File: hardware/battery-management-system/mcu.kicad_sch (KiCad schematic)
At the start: 32 parts, among them J7 ARM-JTAG-SWD, Q6 DMN3404L, Q7 DMN3404L, Q8 DMN3404L, U6 AT24C512C, U7 NCT75DR2G, U8 STM32L071CZTx

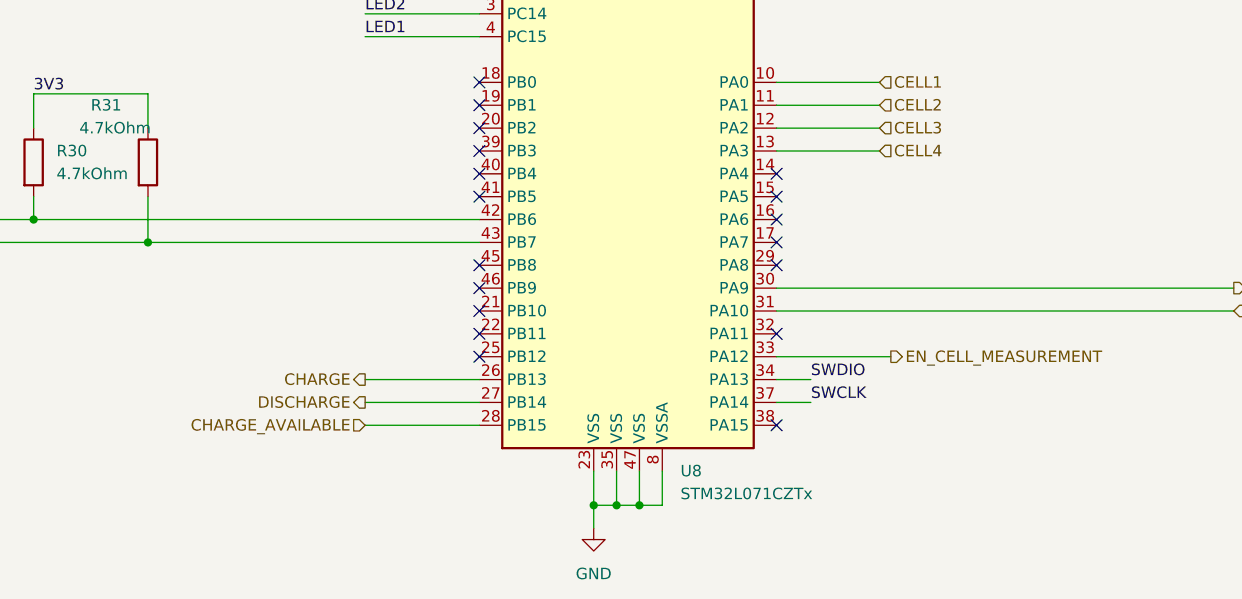
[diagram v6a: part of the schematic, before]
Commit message: finish cell balancing schematic
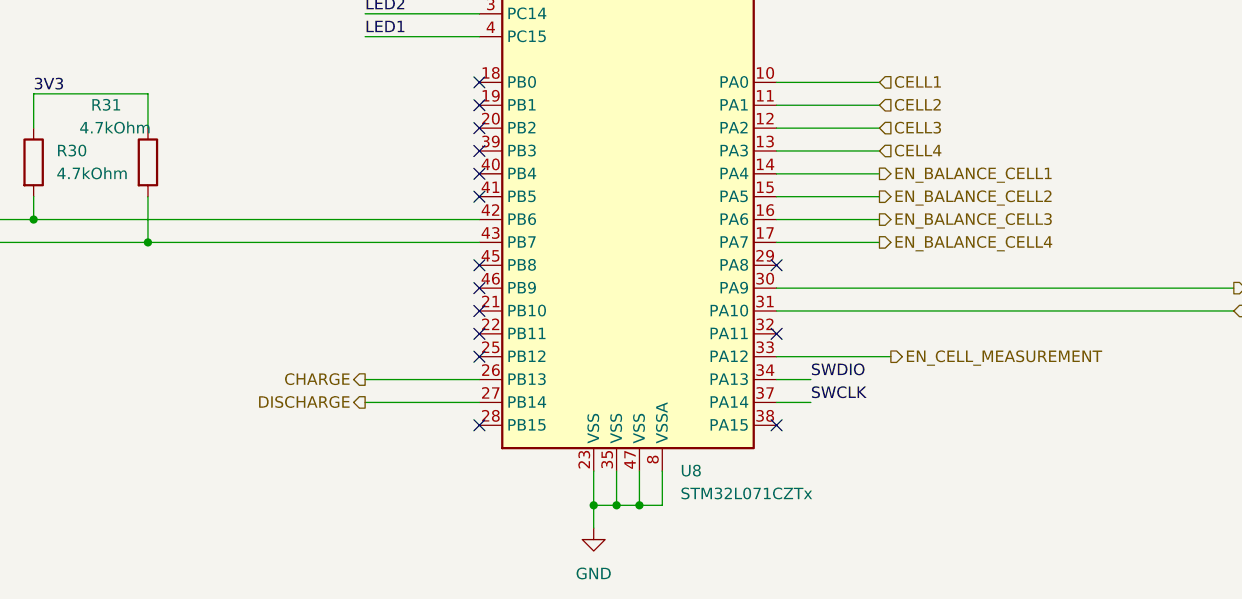
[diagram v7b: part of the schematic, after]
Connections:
- net EN_BALANCE_CELL1: now reaches U8.14 (PA4)
- net EN_BALANCE_CELL2: now reaches U8.15 (PA5)
- net EN_BALANCE_CELL3: now reaches U8.16 (PA6)
- net EN_BALANCE_CELL4: now reaches U8.17 (PA7)
- net CHARGE_AVAILABLE: no longer names the net of U8.28 (PB15)
- no-connect marks 24 -> 21
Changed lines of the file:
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@@
 	)
 	(no_connect
-		(at 27.94 81.28)
+		(at 185.42 104.14)
 	)
 	(no_connect
-		(at 218.44 76.2)
+		(at 27.94 81.28)
 	)
 	(no_connect
@@
 	)
 	(no_connect
-		(at 218.44 83.82)
-	)
-	(no_connect
 		(at 185.42 76.2)
 	)
@@
 	)
 	(no_connect
-		(at 218.44 81.28)
-	)
-	(no_connect
 		(at 218.44 104.14)
 	)
@@
 	)
 	(no_connect
-		(at 218.44 78.74)
-	)
-	(no_connect
 		(at 185.42 48.26)
 	)
@@
 	(wire
 		(pts
+			(xy 218.44 83.82) (xy 229.87 83.82)
+		)
+		(stroke
+			(width 0)
+			(type default)
+		)
+	)
+	(wire
+		(pts
 			(xy 73.66 185.42) (xy 73.66 186.69)
 		)
@@
 	(wire
 		(pts
+			(xy 218.44 78.74) (xy 229.87 78.74)
+		)
+		(stroke
+			(width 0)
+			(type default)
+		)
+	)
+	(wire
+		(pts
 			(xy 90.17 31.75) (xy 102.87 31.75)
 		)
@@
 	(wire
 		(pts
+			(xy 218.44 76.2) (xy 229.87 76.2)
+		)
+		(stroke
+			(width 0)
+			(type default)
+		)
+	)
+	(wire
+		(pts
 			(xy 203.2 113.03) (xy 205.74 113.03)
 		)
@@
 	(wire
 		(pts
+			(xy 218.44 81.28) (xy 229.87 81.28)
+		)
+		(stroke
+			(width 0)
+			(type default)
+		)
+	)
+	(wire
+		(pts
 			(xy 129.54 44.45) (xy 129.54 46.99)
 		)
@@
 	(wire
 		(pts
-			(xy 172.72 104.14) (xy 185.42 104.14)
-		)
-		(stroke
-			(width 0)
-			(type default)
-		)
-	)
-	(wire
-		(pts
 			(xy 83.82 96.52) (xy 83.82 99.06)
 		)
@@
 		)
 	)
-	(hierarchical_label "CHARGE_AVAILABLE"
-		(shape input)
-		(at 172.72 104.14 180)
+	(hierarchical_label "EN_BALANCE_CELL4"
+		(shape output)
+		(at 229.87 83.82 0)
 		(fields_autoplaced yes)
 		(effects
@@
 				(size 1.27 1.27)
 			)
-			(justify right)
+			(justify left)
 		)
 	)
@@
 		)
 	)
+	(hierarchical_label "EN_BALANCE_CELL1"
+		(shape output)
+		(at 229.87 76.2 0)
+		(fields_autoplaced yes)
+		(effects
+			(font
+				(size 1.27 1.27)
+			)
+			(justify left)
+		)
+	)
+	(hierarchical_label "EN_BALANCE_CELL2"
+		(shape output)
+		(at 229.87 78.74 0)
+		(fields_autoplaced yes)
+		(effects
+			(font
+				(size 1.27 1.27)
+			)
+			(justify left)
+		)
+	)
+	(hierarchical_label "EN_BALANCE_CELL3"
+		(shape output)
+		(at 229.87 81.28 0)
+		(fields_autoplaced yes)
+		(effects
+			(font
+				(size 1.27 1.27)
+			)
+			(justify left)
+		)
+	)
 	(symbol
 		(lib_id "benediktibk:C_1uF_SMD_0603_50V_10%")
@@
 			)
 		)
-		(property "Description" ""
+		(property "Description" "Unpolarized capacitor"
 			(at 129.54 40.64 0)
 			(effects
@@
 			)
 		)
-		(property "Description" ""
+		(property "Description" "Special symbol for telling ERC where power comes from"
 			(at 53.34 31.75 0)
 			(effects
@@
 			)
 		)
-		(property "Description" ""
+		(property "Description" "Resistor"
 			(at 97.79 186.69 0)
 			(effects
@@
 			)
 		)
-		(property "Description" ""
+		(property "Description" "Resistor"
 			(at 36.83 168.91 0)
 			(effects
@@
 			)
 		)
-		(property "Description" ""
+		(property "Description" "n-MOSFET transistor, drain/gate/source"
 			(at 34.29 180.34 0)
 			(effects
@@
 			)
 		)
-		(property "Description" ""
+		(property "Description" "Unpolarized capacitor"
 			(at 96.52 90.17 0)
 			(effects
@@
 			)
 		)
-		(property "Description" ""
+		(property "Description" "Light emitting diode"
 			(at 109.22 158.75 0)
 			(effects
@@
 			)
 		)
-		(property "Description" ""
+		(property "Description" "Unpolarized capacitor"
 			(at 64.77 40.64 0)
 			(effects
@@
 			)
 		)
-		(property "Description" ""
+		(property "Description" "Special symbol for telling ERC where power comes from"
 			(at 129.54 31.75 0)
 			(effects
@@
 			)
 		)
-		(property "Description" ""
+		(property "Description" "n-MOSFET transistor, drain/gate/source"
 			(at 106.68 180.34 0)
 			(effects
@@
 			)
 		)
-		(property "Description" ""
+		(property "Description" "Power symbol creates a global label with name \"GND\" , ground"
 			(at 36.83 189.23 0)
 			(effects
@@
 			)
 		)
-		(property "Description" ""
+		(property "Description" "Resistor"
 			(at 177.8 43.18 0)
 			(effects
@@
 			)
 		)
-		(property "Description" ""
+		(property "Description" "Power symbol creates a global label with name \"GND\" , ground"
 			(at 73.66 189.23 0)
 			(effects
@@
 			)
 		)
-		(property "Description" ""
+		(property "Description" "Power symbol creates a global label with name \"GND\" , ground"
 			(at 74.93 138.43 0)
 			(effects
@@
 			)
 		)
-		(property "Description" ""
+		(property "Description" "Power symbol creates a global label with name \"GND\" , ground"
 			(at 129.54 49.53 0)
 			(effects
@@
 			)
 		)
-		(property "Description" ""
+		(property "Description" "Resistor"
 			(at 135.89 74.93 0)
 			(effects
@@
 			)
 		)
-		(property "Description" ""
+		(property "Description" "Resistor"
 			(at 73.66 168.91 0)
 			(effects
@@
 			)
 		)
-		(property "Description" ""
+		(property "Description" "Unpolarized capacitor"
 			(at 90.17 40.64 0)
 			(effects
@@
 			)
 		)
-		(property "Description" ""
+		(property "Description" "Single Pole Single Throw (SPST) switch"
 			(at 83.82 91.44 0)
 			(effects
@@
 			)
 		)
-		(property "Description" ""
+		(property "Description" "Power symbol creates a global label with name \"GND\" , ground"
 			(at 109.22 189.23 0)
 			(effects
@@
 			)
 		)
-		(property "Description" ""
+		(property "Description" "Power symbol creates a global label with name \"GND\" , ground"
 			(at 24.13 86.36 0)
 			(effects
@@
 			)
 		)
-		(property "Description" ""
+		(property "Description" "Unpolarized capacitor"
 			(at 77.47 40.64 0)
 			(effects
@@
 			)
 		)
-		(property "Description" ""
+		(property "Description" "Unpolarized capacitor"
 			(at 116.84 40.64 0)
 			(effects
@@
 			)
 		)
-		(property "Description" ""
+		(property "Description" "Resistor"
 			(at 62.23 186.69 0)
 			(effects
@@
 			)
 		)
-		(property "Description" ""
+		(property "Description" "Resistor"
 			(at 25.4 186.69 0)
 			(effects
@@
 			)
 		)
-		(property "Description" ""
+		(property "Description" "Resistor"
 			(at 148.59 74.93 0)
 			(effects
@@
 			)
 		)
-		(property "Description" ""
+		(property "Description" "Power symbol creates a global label with name \"GND\" , ground"
 			(at 198.12 115.57 0)
 			(effects
@@
 			)
 		)
-		(property "Description" ""
+		(property "Description" "n-MOSFET transistor, drain/gate/source"
 			(at 71.12 180.34 0)
 			(effects
@@
 			)
 		)
-		(property "Description" ""
+		(property "Description" "Unpolarized capacitor"
 			(at 74.93 123.19 0)
 			(effects
@@
 			)
 		)
-		(property "Description" ""
+		(property "Description" "ARM Cortex-M0+ MCU, 192KB flash, 20KB RAM, 32MHz, 1.65-3.6V, 37 GPIO, LQFP-48"
 			(at 203.2 71.12 0)
 			(effects
@@
 			)
 		)
-		(property "Description" ""
+		(property "Description" "Power symbol creates a global label with name \"GND\" , ground"
 			(at 148.59 46.99 0)
 			(effects
@@
 			)
 		)
-		(property "Description" ""
+		(property "Description" "Light emitting diode"
 			(at 73.66 158.75 0)
 			(effects
@@
 			)
 		)
-		(property "Description" ""
+		(property "Description" "Light emitting diode"
 			(at 36.83 158.75 0)
 			(effects
@@
 			)
 		)
-		(property "Description" ""
+		(property "Description" "Power symbol creates a global label with name \"GND\" , ground"
 			(at 30.48 140.97 0)
 			(effects
@@
 			)
 		)
-		(property "Description" ""
+		(property "Description" "Resistor"
 			(at 109.22 168.91 0)
 			(effects
@@
 			)
 		)
-		(property "Description" ""
+		(property "Description" "I2C Serial EEPROM, 2Kb, SOT-23"
 			(at 93.98 124.46 0)
 			(effects
@@
 			)
 		)
-		(property "Description" ""
+		(property "Description" "Resistor"
 			(at 80.01 69.85 0)
 			(effects
@@
 			)
 		)
-		(property "Description" ""
+		(property "Description" "Power symbol creates a global label with name \"GND\" , ground"
 			(at 53.34 49.53 0)
 			(effects
@@
 			)
 		)
-		(property "Description" ""
+		(property "Description" "I2C Serial EEPROM, 2Kb, SOT-23"
 			(at 49.53 123.19 0)
 			(effects
@@
 			)
 		)
-		(property "Description" ""
+		(property "Description" "Unpolarized capacitor"
 			(at 30.48 121.92 0)
 			(effects
@@
 			)
 		)
-		(property "Description" ""
+		(property "Description" "Ferrite bead"
 			(at 110.49 31.75 0)
 			(effects
@@
 			)
 		)
-		(property "Description" ""
+		(property "Description" "Unpolarized capacitor"
 			(at 53.34 40.64 0)
 			(effects
@@
 			)
 		)
-		(property "Description" ""
+		(property "Description" "Unpolarized capacitor"
 			(at 102.87 40.64 0)
 			(effects
@@
 			)
 		)
-		(property "Description" ""
+		(property "Description" "Power symbol creates a global label with name \"GND\" , ground"
 			(at 96.52 101.6 0)
 			(effects

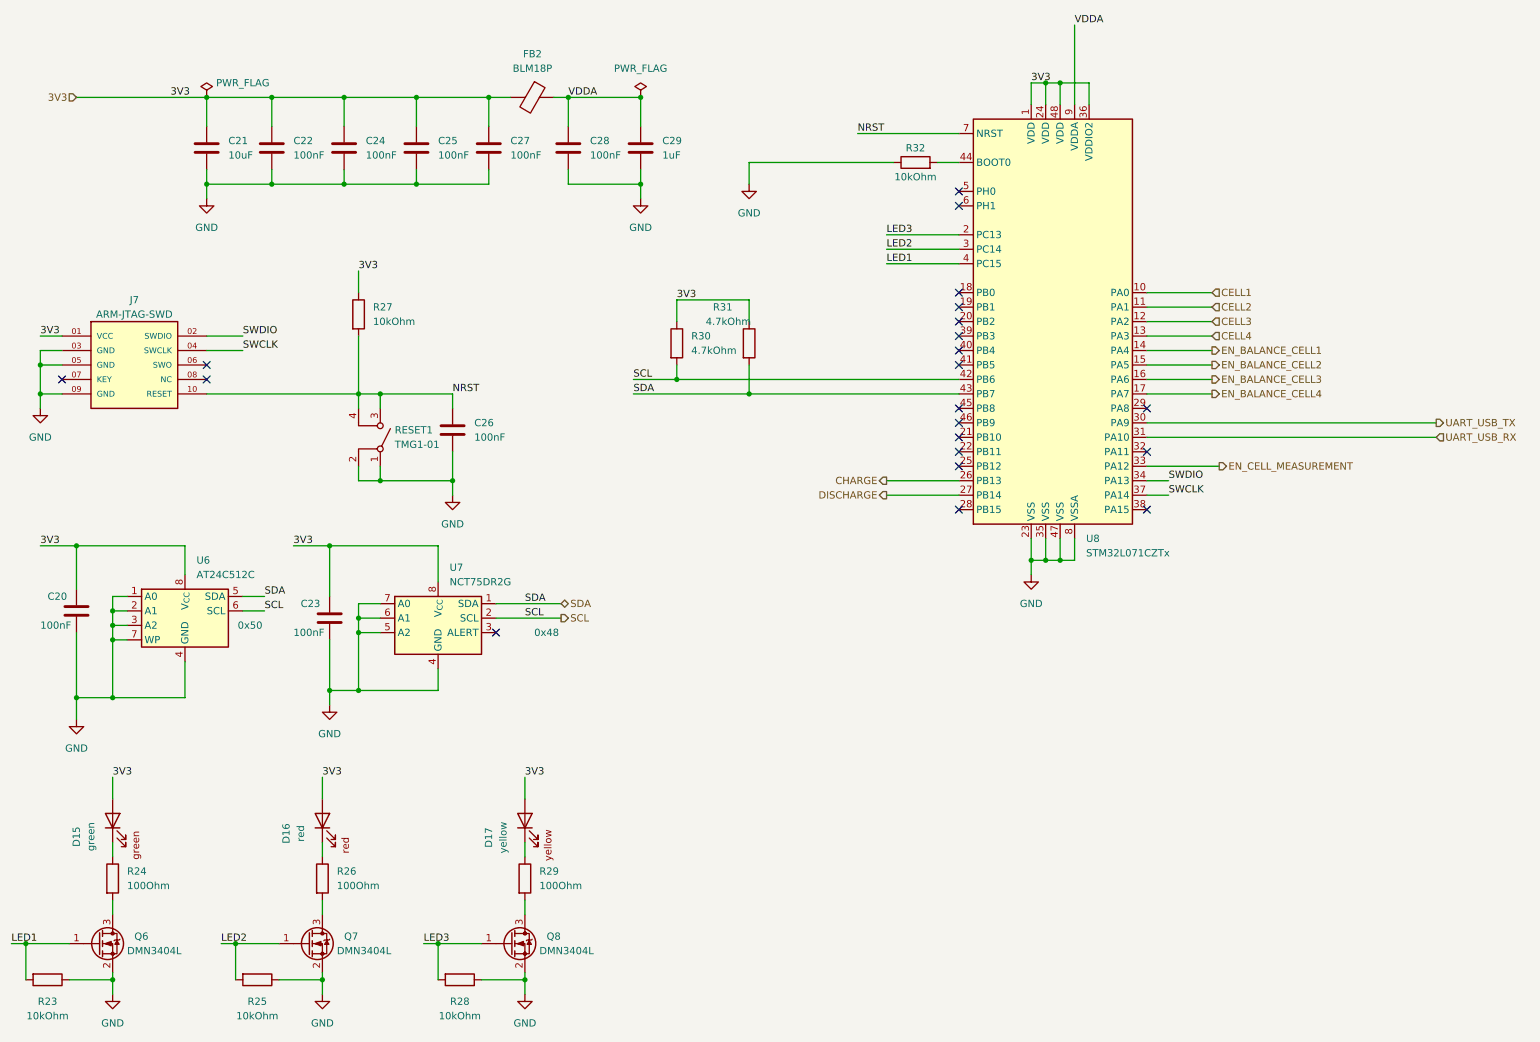
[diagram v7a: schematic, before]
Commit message: add snubber circuit
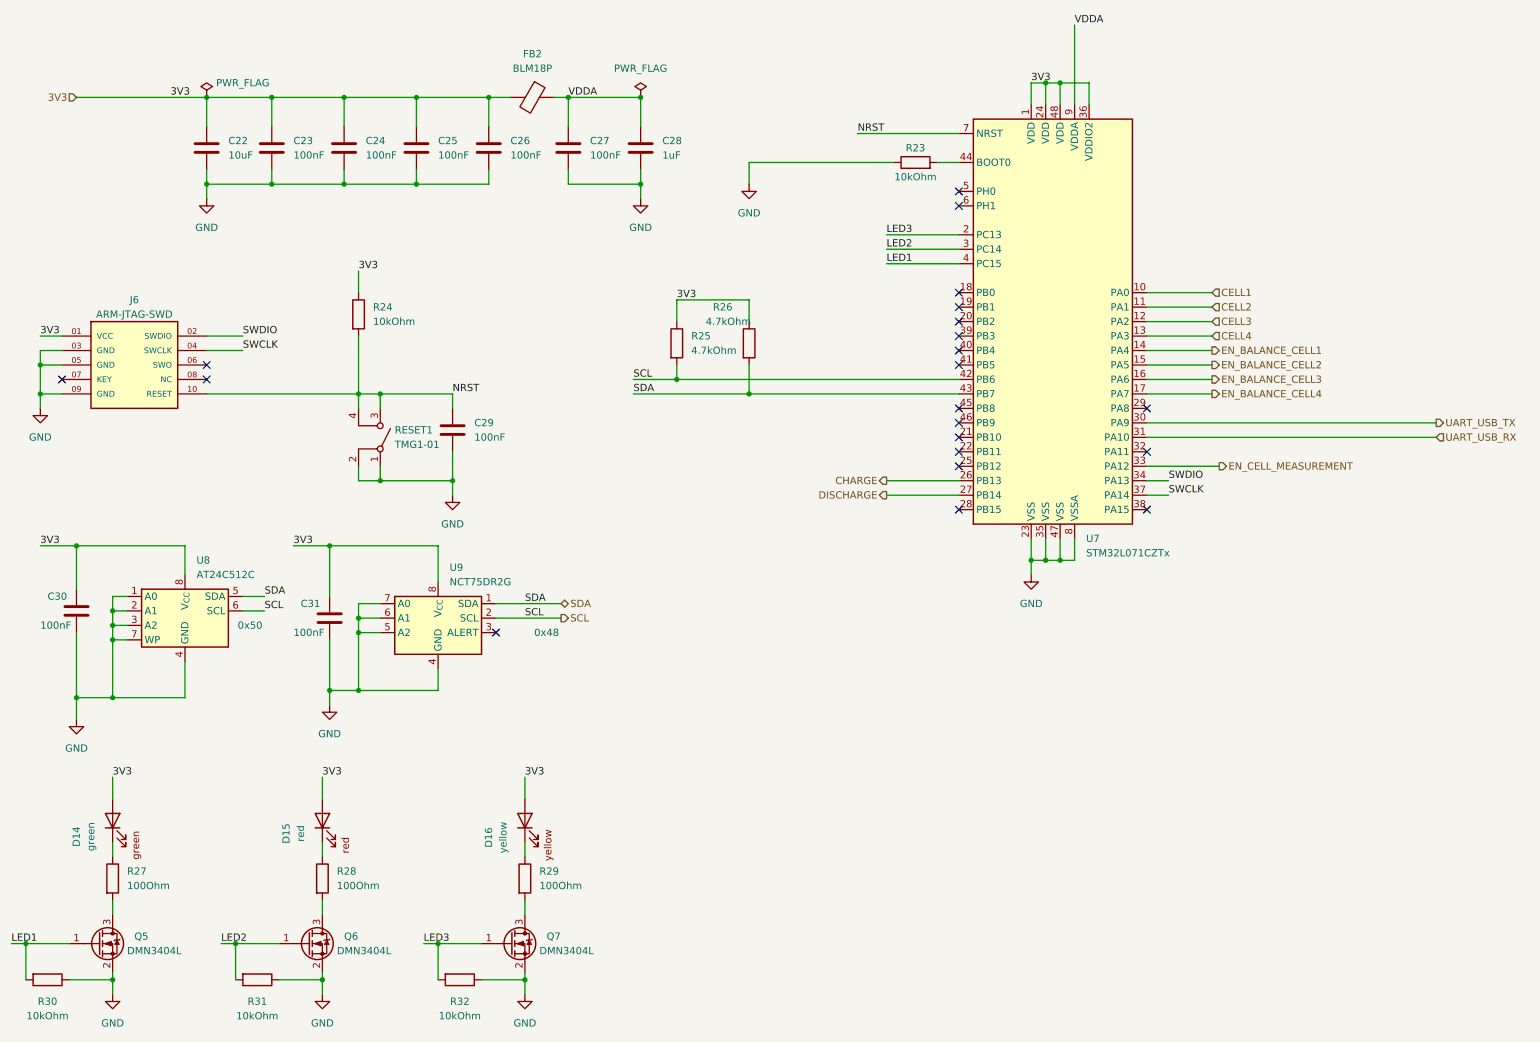
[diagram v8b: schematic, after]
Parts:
- renumbered C21 to C22, C22 to C23, C27 to C26, C28 to C27, C29 to C28, C26 to C29, C20 to C30, C23 to C31, D15 to D14, D16 to D15, D17 to D16, J7 to J6, Q6 to Q5, Q7 to Q6, Q8 to Q7, R32 to R23, R27 to R24, R30 to R25, R31 to R26, R24 to R27, R26 to R28, R23 to R30, R25 to R31, R28 to R32, U8 to U7, U6 to U8, U7 to U9
